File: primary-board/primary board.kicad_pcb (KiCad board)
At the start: 4 copper layers, 92 x 82 mm, 44 parts, among them J1 USB_C, J10 Motor Connector Right, J2 Sensor_Forward, J3 Sensor_Right, J4 Sensor_Left, J5 I2C Breakout, J6 Conn_01x02, J7 Conn_01x02, J8 Conn_01x02, J9 Motor Connector Left, SW1 SW_SPST, SW2 SW_SPST, U1 ESP32-S3-1, U2 L7806, U3 L7806, U4 AZ1117-3.3, U5 DRV8411ARTER

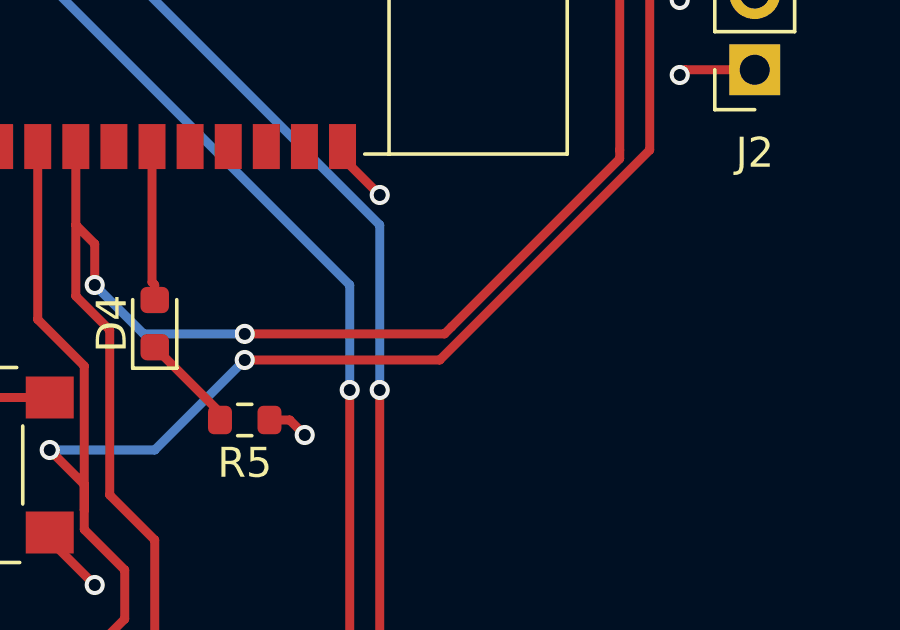
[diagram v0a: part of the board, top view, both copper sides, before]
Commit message: added i2c pullups
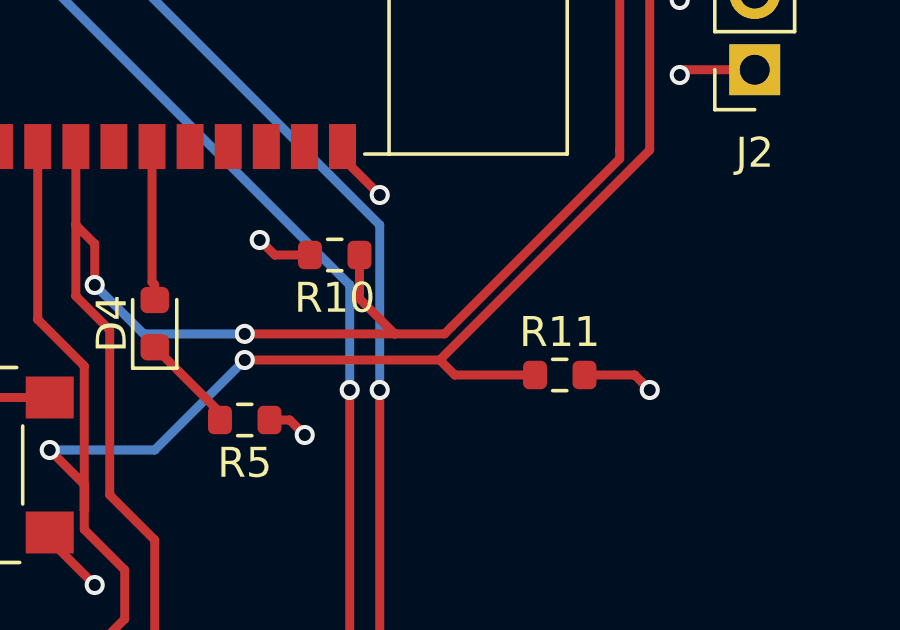
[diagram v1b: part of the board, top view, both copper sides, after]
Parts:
- added R10: 10k, Resistor_SMD:R_0603_1608Metric, F.Cu at (176.5, 101.5)
- added R11: 10k, Resistor_SMD:R_0603_1608Metric, F.Cu at (184.0, 105.5)
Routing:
- net +3.3V: track 34.1 -> 38.4 mm, vias 12 -> 14
- net /MCU_SCL: track 125.1 -> 128.5 mm
- net /MCU_SDA: track 119.8 -> 122.9 mm

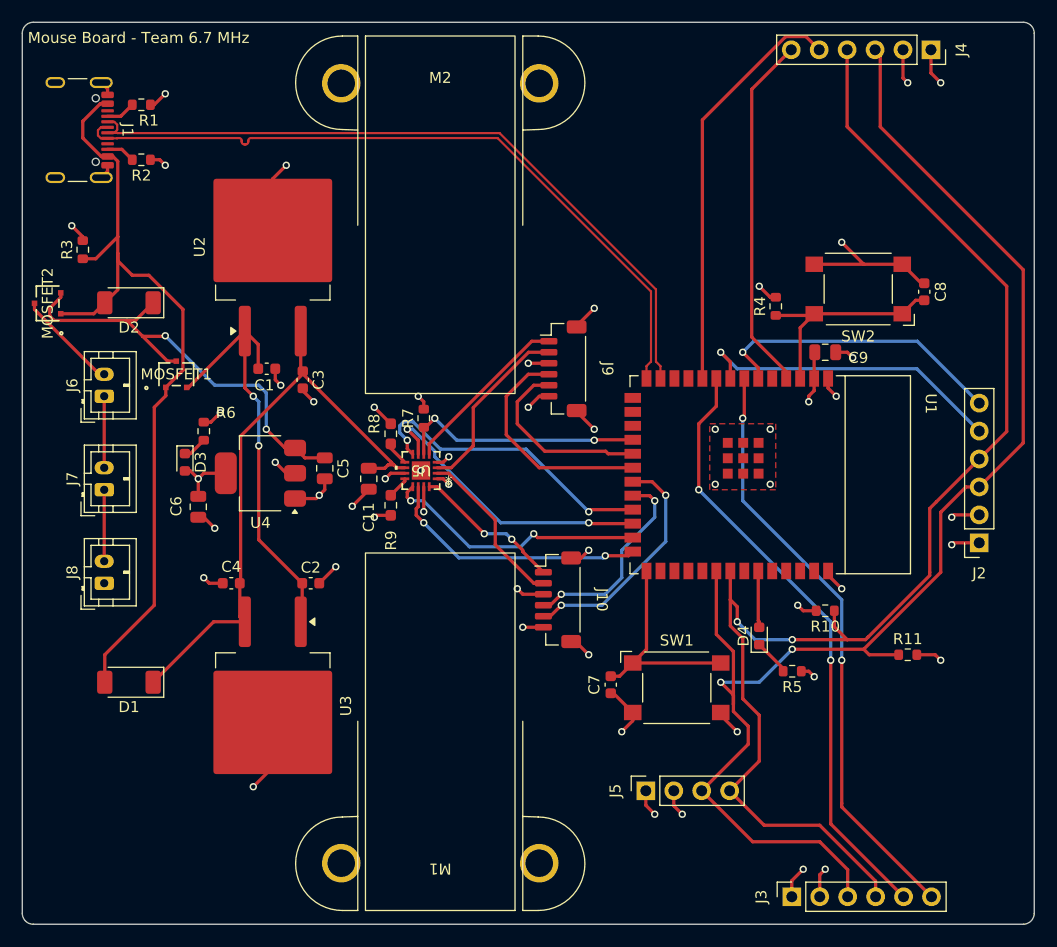
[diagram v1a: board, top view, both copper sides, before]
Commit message: adjusted drv8821 paste, added fiducials
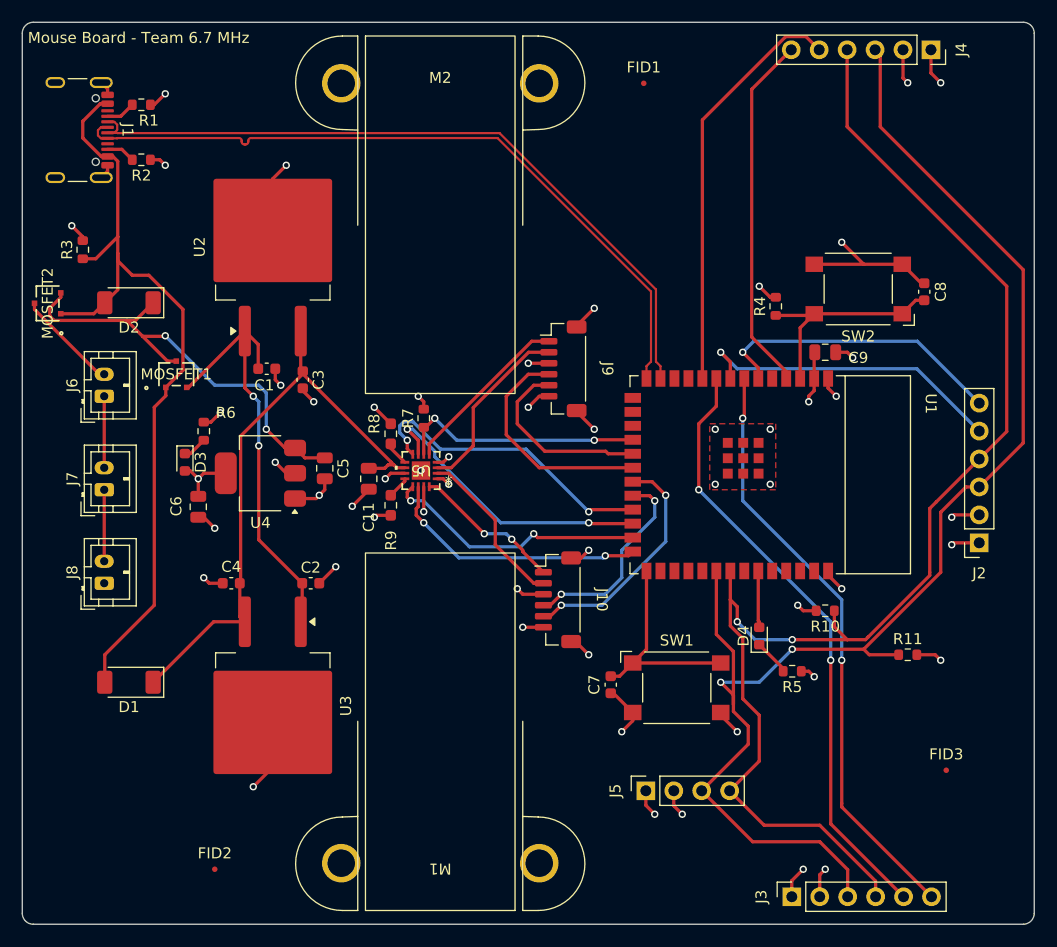
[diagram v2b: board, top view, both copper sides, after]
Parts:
- added FID1: Fiducial, Fiducial:Fiducial_0.5mm_Mask1mm, F.Cu at (160.0, 53.5)
- added FID2: Fiducial, Fiducial:Fiducial_0.5mm_Mask1mm, F.Cu at (121.0, 125.0)
- added FID3: Fiducial, Fiducial:Fiducial_0.5mm_Mask1mm, F.Cu at (187.5, 116.0)
